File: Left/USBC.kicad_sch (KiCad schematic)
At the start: 5 parts, among them J1 USB-C USB 2.0 MC-372, U28 USBLC6-2SC6

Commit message: Finished left hand
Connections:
- no-connect marks 1 -> 4
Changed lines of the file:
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@@
   (junction (at 111.76 91.44) (diameter 0) (color 0 0 0 0)
   )
-  (no_connect (at 86.36 115.57))
+  (no_connect (at 87.63 115.57))
+  (no_connect (at 85.725 115.57))
+  (no_connect (at 91.44 115.57))
+  (no_connect (at 89.535 115.57))
   (wire (pts (xy 112.014 96.52) (xy 111.76 96.647))
     (stroke (width 0) (type default) (color 0 0 0 0))
@@
     (pin "B7")
     (pin "S1")
+    (pin "S2")
+    (pin "S3")
+    (pin "S4")
   )
   (symbol (lib_id "Device:R") (at 111.125 113.792 0) (unit 1)

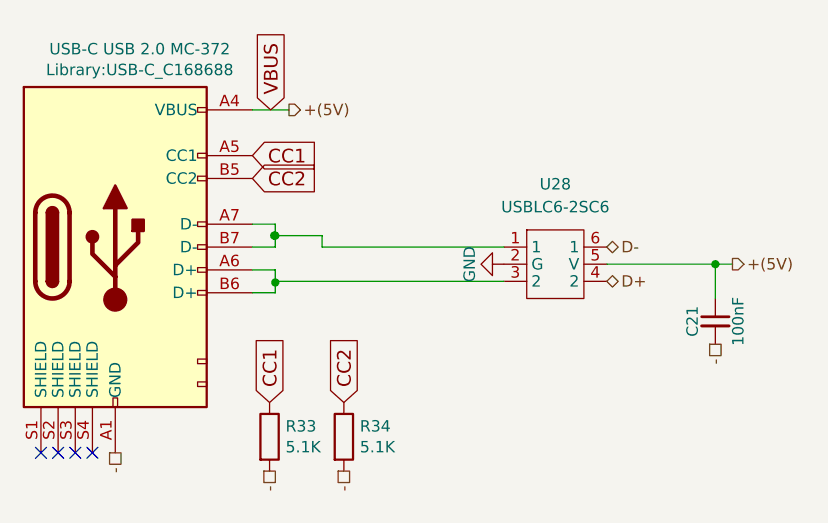
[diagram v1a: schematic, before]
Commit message: upgraded files to kicad7
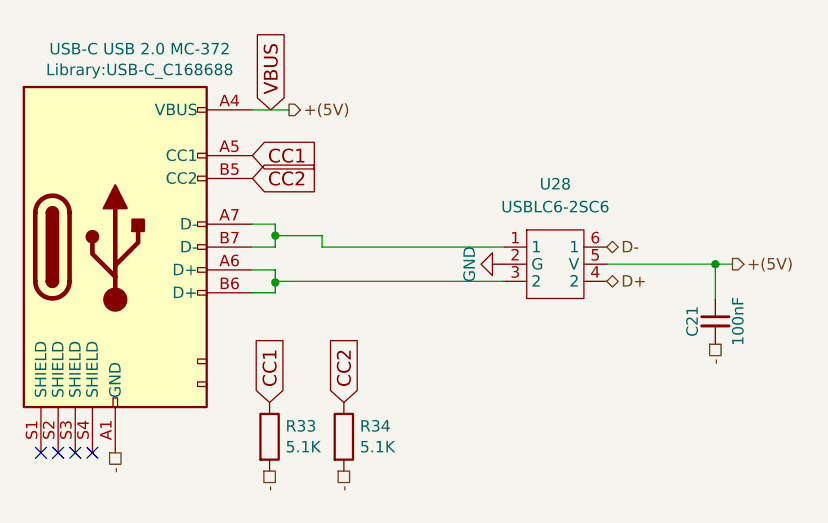
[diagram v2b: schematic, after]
